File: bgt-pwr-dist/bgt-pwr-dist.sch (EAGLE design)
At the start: 29 parts

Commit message: bgt-prw-dist: various small fixes
* update littelfuse library for 0.9mm drill (instead of 0.8mm)
* increase restring sizes
* increase trace width from 2mm to 2.54mm
* 10mm THT resistor instead of 7mm
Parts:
- R1, R2: device resistor:R-EU_0207/7 -> resistor:R-EU_0207/10
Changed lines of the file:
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@@
 <part name="GND5" library="supply1" deviceset="GND" device=""/>
 <part name="GND6" library="supply1" deviceset="GND" device=""/>
-<part name="R1" library="resistor" deviceset="R-EU_" device="0207/7"/>
-<part name="R2" library="resistor" deviceset="R-EU_" device="0207/7"/>
+<part name="R1" library="resistor" deviceset="R-EU_" device="0207/10"/>
+<part name="R2" library="resistor" deviceset="R-EU_" device="0207/10"/>
 <part name="P+4" library="supply1" deviceset="VCC" device=""/>
 </parts>

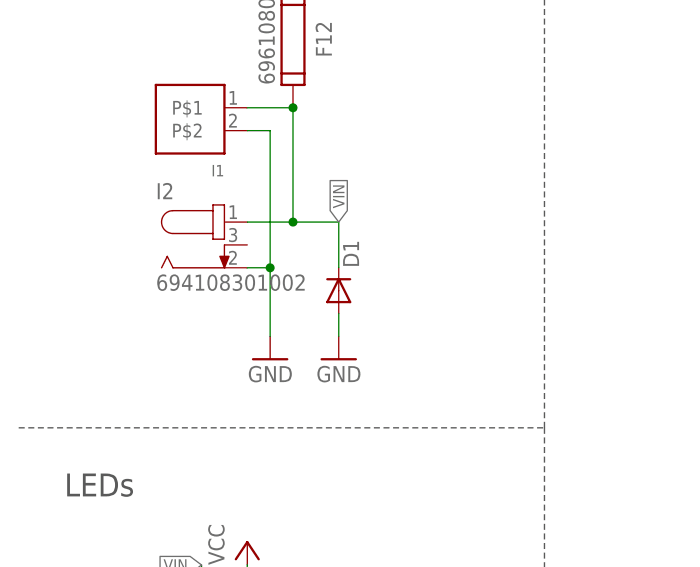
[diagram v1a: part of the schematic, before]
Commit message: bgt-pwr-dist: Finalize v2
* no milling for DC jack (cheaper PCB production)
* update version to v2
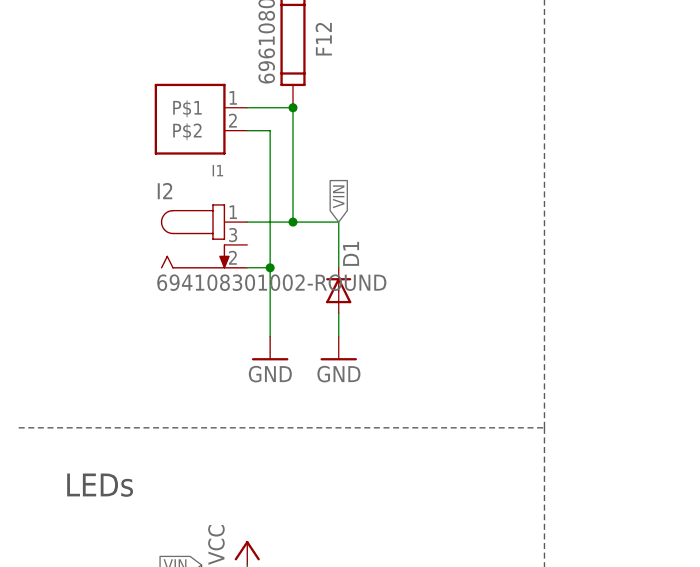
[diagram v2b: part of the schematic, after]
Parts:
- I2: value 694108301002 -> 694108301002-ROUND; device Wurth_Elektronik_Electromechanic_DC_Power_Jack_Connectors_rev15c:694108301002 -> Wurth_Elektronik_Electromechanic_DC_Power_Jack_Connectors_rev15c:694108301002-ROUND
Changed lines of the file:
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@@
 <part name="P+1" library="supply1" deviceset="VCC" device=""/>
 <part name="I1" library="RIA-PlugCon" deviceset="RIA_1X2" device="-230"/>
-<part name="I2" library="Wurth_Elektronik_Electromechanic_DC_Power_Jack_Connectors_rev15c" deviceset="694108301002" device=""/>
+<part name="I2" library="Wurth_Elektronik_Electromechanic_DC_Power_Jack_Connectors_rev15c" deviceset="694108301002" device="-ROUND" value="694108301002-ROUND"/>
 <part name="GND2" library="supply1" deviceset="GND" device=""/>
 <part name="P+2" library="supply1" deviceset="VCC" device=""/>

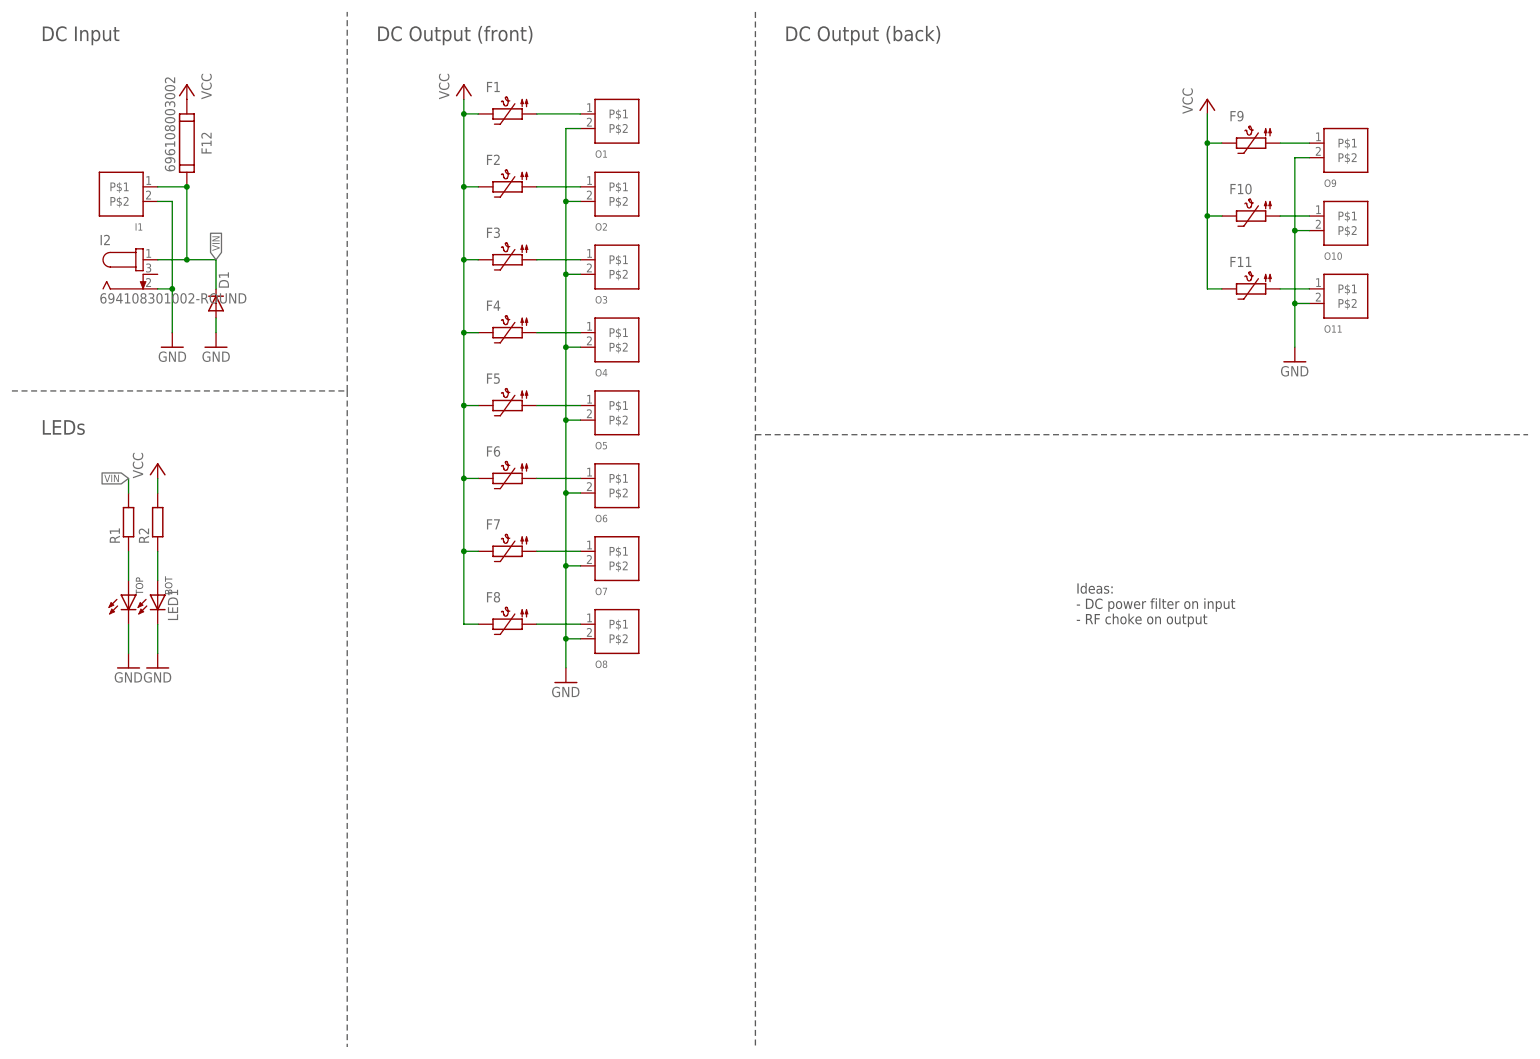
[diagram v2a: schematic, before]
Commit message: bgt-pwr-dist: Part attribute annotation for BOM generation
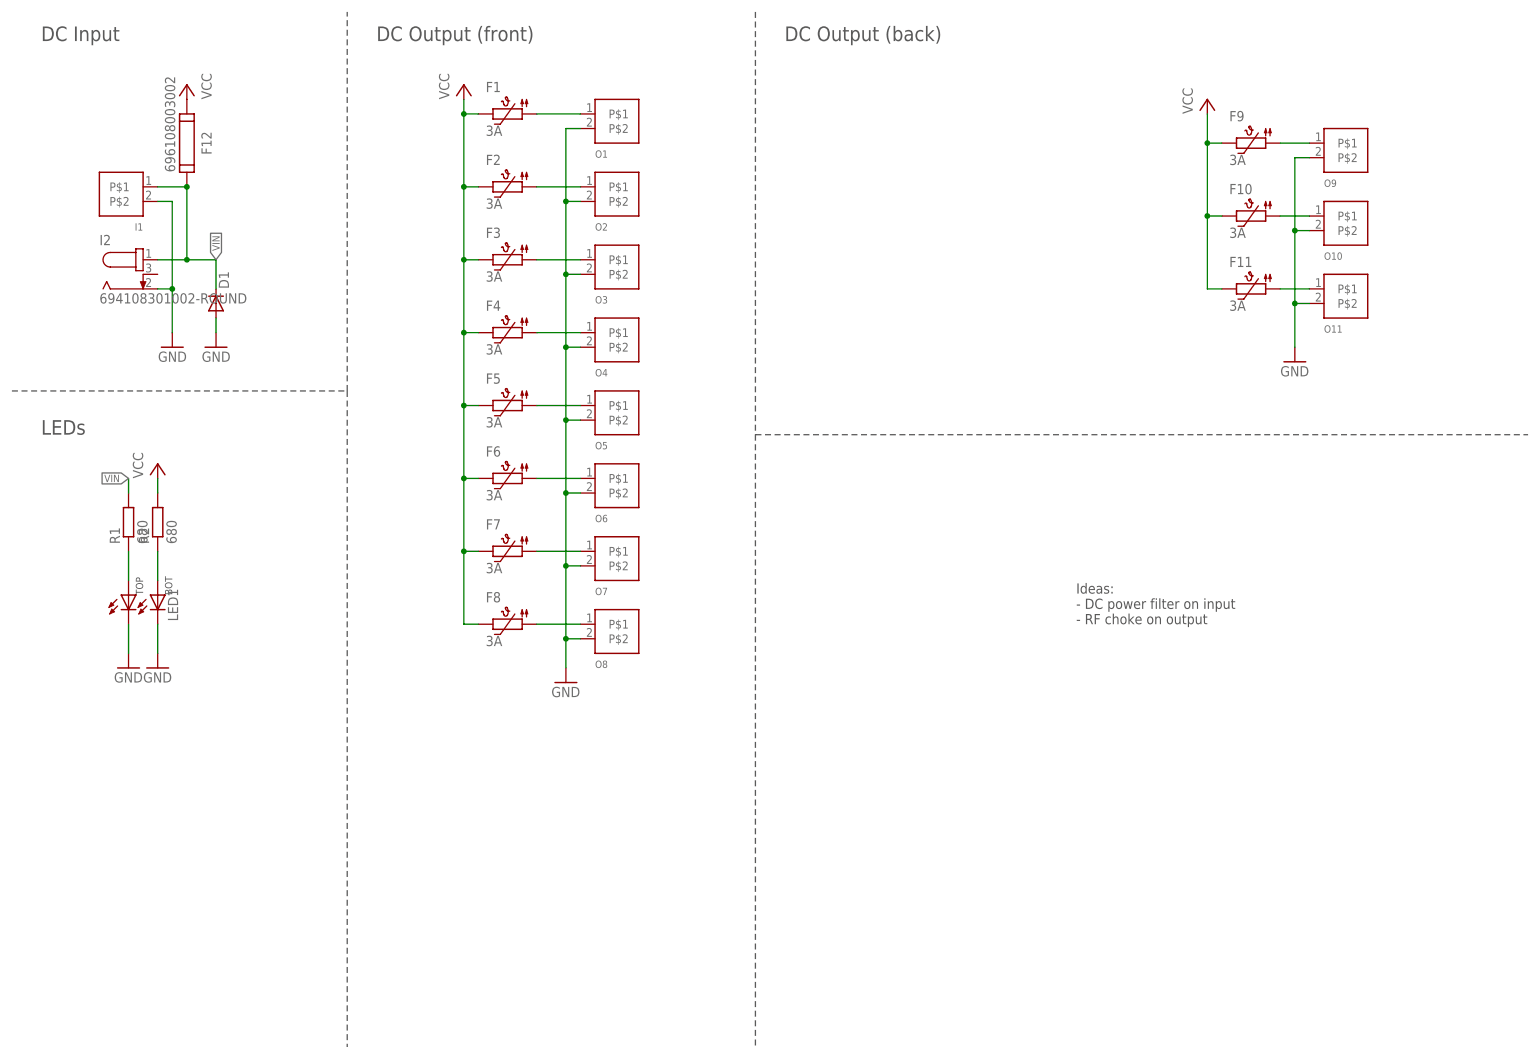
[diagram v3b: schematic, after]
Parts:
- D1: CLASS (none) -> DIODE; DESCRIPTION (none) -> DIODE ZENER 14V 5W DO15; LINK (none) -> https://www.digikey.de/en/products/detail/micro-commercial-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; MANUFACTURER (none) -> Micro Commercial Co; MANUFACTURERPARTNUMBER (none) -> 1N5351B; POPULATED (none) -> TRUE; ROHSCERTIFICATE (none) -> UNKNOWN ROHS CERTIFICATE; SOURCE (none) -> DIGIKEY; SOURCEPARTNUMBER (none) -> 1N5351BTPMSCT-ND
- F1, F10, F11, F2, F3, F4, F5, F6, F7, F8, F9: value (none) -> 3A; CLASS (none) -> UNKNOWN CLASS; DESCRIPTION (none) -> PTC RESET FUSE 16V 3A RADIAL; LINK (none) -> https://www.digikey.de/en/products/detail/littelfuse-inc/16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; MANUFACTURER (none) -> LITTELFUSE; MANUFACTURERPARTNUMBER (none) -> 16R300GPR; POPULATED (none) -> TRUE; ROHSCERTIFICATE (none) -> UNKNOWN ROHS CERTIFICATE; SOURCE (none) -> DIGIKEY; SOURCEPARTNUMBER (none) -> 18-16R300GPRCT-ND
- F12: CLASS (none) -> UNKNOWN CLASS; DESCRIPTION (none) -> FUSEHOLDER BLOCKS - PCB - CLIP C; LINK (none) -> https://www.digikey.de/en/products/detail/w%C3%BCrth-elektr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; MANUFACTURER (none) -> Wuerth Elektronik; MANUFACTURERPARTNUMBER (none) -> 696108003002; POPULATED (none) -> TRUE; ROHSCERTIFICATE (none) -> UNKNOWN ROHS CERTIFICATE; SOURCE (none) -> DIGIKEY; SOURCEPARTNUMBER (none) -> 732-11376-ND
- I1: CLASS (none) -> UNKNOWN CLASS; DESCRIPTION (none) -> NO DESCRIPTION; LINK (none) -> https://www.digikey.de/en/products/detail/cui-devices/TBP01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; MANUFACTURER (none) -> CUI Devices; MANUFACTURERPARTNUMBER (none) -> TBP01R1-508-02BE; POPULATED (none) -> TRUE; ROHSCERTIFICATE (none) -> UNKNOWN ROHS CERTIFICATE; SOURCE (none) -> DIGIKEY; SOURCEPARTNUMBER (none) -> 102-6406-ND
- I2: CLASS (none) -> UNKNOWN CLASS; DESCRIPTION (none) -> CONN PWR JACK 2.5X5.5MM SOLDER; LINK (none) -> https://www.digikey.de/en/products/detail/w%C3%BCrth-elektr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; MANUFACTURER (none) -> Würth Elektronik; MANUFACTURERPARTNUMBER (none) -> 694108301002; POPULATED (none) -> TRUE; ROHSCERTIFICATE (none) -> UNKNOWN ROHS CERTIFICATE; SOURCE (none) -> DIGIKEY; SOURCEPARTNUMBER (none) -> 732-5934-ND
- LED1: CLASS (none) -> LED; DESCRIPTION (none) -> LED 3MM BI-LEVEL 565NM GRN DIFF; LINK (none) -> https://www.digikey.de/en/products/detail/kingbright/WP934M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; MANUFACTURER (none) -> Kingbright; MANUFACTURERPARTNUMBER (none) -> WP934MD/2GD; POPULATED (none) -> TRUE; ROHSCERTIFICATE (none) -> UNKNOWN ROHS CERTIFICATE; SOURCE (none) -> DIGIKEY; SOURCEPARTNUMBER (none) -> 754-1748-ND
- O1, O10, O11, O2, O3, O4, O5, O6, O7, O8, O9: CLASS (none) -> UNKNOWN CLASS; DESCRIPTION (none) -> NO DESCRIPTION; LINK (none) -> https://www.digikey.de/en/products/detail/cui-devices/TBP02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; MANUFACTURER (none) -> CUI DEVICES; MANUFACTURERPARTNUMBER (none) -> TBP02R1-381-02BE; POPULATED (none) -> TRUE; ROHSCERTIFICATE (none) -> UNKNOWN ROHS CERTIFICATE; SOURCE (none) -> DIGIKEY; SOURCEPARTNUMBER (none) -> 102-6480-ND
- R1, R2: value (none) -> 680; CLASS (none) -> RESISTOR; DESCRIPTION (none) -> RES 680 OHM 5% 1/4W AXIAL; LINK (none) -> https://www.digikey.de/en/products/detail/stackpole-electro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; MANUFACTURER (none) -> UNKNOWN MANUFACTURER; MANUFACTURERPARTNUMBER (none) -> CF14JT680R; POPULATED (none) -> TRUE; ROHSCERTIFICATE (none) -> Stackpole; SOURCE (none) -> DIGIKEY; SOURCEPARTNUMBER (none) -> CF14JT680RCT-ND
